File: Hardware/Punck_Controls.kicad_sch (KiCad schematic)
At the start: 34 parts, among them J1 Audio_In_L, J11 Conn_01x08_Female, J12 Conn_01x08_Female, J13 Conn_01x08_Female, J14 Conn_01x08_Female, J4 Audio_Out_R, J8 Audio_Out_L

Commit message: Rough Draft of Control PCB Done
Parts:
- removed BTN1, BTN2, BTN3, BTN4, BTN5, BTN6: SW_Push, Custom_Footprints:SW_PUSH_6mm_aligned, symbol Switch:SW_Push
- removed D?: LED_Dual_AKA, LED_THT:LED_D3.0mm-3, symbol Device:LED_Dual_AKA
- removed J11, J12, J13, J14: Conn_01x08_Female, Socket_Strips:Socket_Strip_Straight_1x08_Pitch2.54mm, symbol Connector:Conn_01x08_Female
- removed R? (x2): 1k, Resistor_SMD:R_0603_1608Metric, symbol Device:R_Small
- removed Snare_Decay_Pot1, Toms_Vol_Pot: B10k, Custom_Footprints:Alpha_9mm_Potentiometer_Aligned, symbol Device:R_POT
- added BTN1, BTN2, BTN3, BTN4, BTN5, BTN6: KS01-BLV, Custom_Footprints:KS01-BLV, symbol LED_Button_KS01-BLV:KS01-BLV
- added J1: (no value), symbol Connector:Conn_01x12_Female
- added J2, J3, J4: Conn_01x12_Female, symbol Connector:Conn_01x12_Female
- added J? (x5): (no value), Custom_Footprints:THONKICONN_hole, symbol thonkiconn:AudioJack2_Ground_Switch
- added SampleA_Voice_Pot1, SampleB_Voice_Pot1: B10k, Custom_Footprints:Alpha_9mm_Potentiometer_Aligned, symbol Device:R_POT
- J7: renamed from J1; value Audio_In_L -> Midi_In_L
- gave numbers to parts that had none: 7
- renumbered HiHat_Decay_Pot to HiHat_Decay_Pot1, J4 to J5, Kick_Filter_Pot1 to Kick_Attack_Pot1, Kick_Decay1 to Kick_Decay_Pot1, Sample_Speed_Pot1 to SampleB_Speed_Pot1
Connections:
- net +3.3VA: now also J1.1 (Pin_1), SampleA_Voice_Pot1.1, SampleB_Voice_Pot1.1
- net EXT_AUDIO_OUT_L: now also J4.11 (Pin_11)
- net EXT_AUDIO_OUT_R: now also J4.10 (Pin_10)
- net GND: now also BTN1.3, BTN1.4, BTN1.6 (K), BTN2.3, BTN2.4, BTN2.6 (K), BTN3.3, BTN3.4, BTN3.6 (K), BTN4.3, BTN4.4, BTN4.6 (K), BTN5.3, BTN5.4, BTN5.6 (K), BTN6.3, BTN6.4, BTN6.6 (K), J4.12 (Pin_12), J?.1, J?.1, J?.1, J?.1, J?.1, J?.2, J?.2, J?.2, J?.2, J?.2, SampleA_Voice_Pot1.3, SampleB_Voice_Pot1.3
- net HIHAT_DECAY_POT: now also J3.3 (Pin_3)
- net HIHAT_VOL_POT: now also J3.4 (Pin_4)
- net KICK_DECAY_POT: now also J2.6 (Pin_6)
- net KICK_VOL_POT: now also J2.7 (Pin_7)
- net MIDI_IN: now also J4.6 (Pin_6)
- net MIDI_LEARN: now also J4.7 (Pin_7)
- net SAMPLER_A_SPEED_POT: now also J3.6 (Pin_6)
- net SAMPLER_A_VOL_POT: now also J3.7 (Pin_7)
- net SAMPLER_B_SPEED_POT: now also J3.9 (Pin_9)
- net SAMPLER_B_VOL_POT: now also J3.10 (Pin_10)
- net SEQ_SELECT: now also J4.8 (Pin_8)
- net SNARE_FILTER_POT: now also J2.8 (Pin_8)
- net SNARE_TUNING_POT: now also J2.9 (Pin_9)
- net SNARE_VOL_POT: now also J2.10 (Pin_10)
- net TEMPO: now also J4.9 (Pin_9)
- net USB_DM: now also J4.4 (Pin_4)
- net USB_DP: now also J4.3 (Pin_3)
- net USB_VBUS: now also J4.5 (Pin_5)
- net KICK_FILTER_POT renamed KICK_ATTACK_POT
- net KICK_ATTACK_POT: now also J2.5 (Pin_5)
- new net CH_BTN: BTN3.1, BTN3.2, J1.7 (Pin_7)
- new net CH_LED: BTN3.5 (A), J1.8 (Pin_8)
- new net KICK_IN: J1.2 (Pin_2), J?.3
- new net KI_BTN: BTN1.1, BTN1.2
- new net KI_LED: BTN1.5 (A)
- new net OH_BTN: BTN6.1, BTN6.2, J1.5 (Pin_5)
- new net OH_IN: J2.2 (Pin_2), J?.3
- new net OH_LED: BTN6.5 (A), J1.6 (Pin_6)
- new net SAMPLERA_IN: J3.2 (Pin_2), J?.3
- new net SAMPLERB_IN: J4.2 (Pin_2), J?.3
- new net SAMPLER_A_VOICE_POT: J3.5 (Pin_5), SampleA_Voice_Pot1.2
- new net SAMPLER_B_VOICE_POT: J3.8 (Pin_8), SampleB_Voice_Pot1.2
- new net SA_BTN: BTN4.1, BTN4.2, J1.9 (Pin_9)
- new net SA_LED: BTN4.5 (A), J1.10 (Pin_10)
- new net SB_BTN: BTN5.1, BTN5.2, J2.3 (Pin_3)
- new net SB_LED: BTN5.5 (A), J2.4 (Pin_4)
- new net SNARE_IN: J1.11 (Pin_11), J?.3
- new net SN_BTN: BTN2.1, BTN2.2, J1.3 (Pin_3)
- new net SN_LED: BTN2.5 (A), J1.4 (Pin_4)
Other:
- note added: "System Controls"
- note added: "Voice Controls"
- note removed: "CV Inputs"
- note removed: "Switches and Buttons"
- moved on the sheet: BTN_MODE1, HiHat_Decay_Pot1, HiHat_Level_Pot1, J5, J6, J7, J8, Kick_Attack_Pot1, Kick_Decay_Pot1, Kick_Level_Pot1, RESET1, SampleA_Level_Pot1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

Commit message: First draft of Controls PCB
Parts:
- added J15: Audio_Out_R, Custom_Footprints:THONKICONN_hole, symbol thonkiconn:AudioJack2_Ground_Switch
- added J7: OH_In, Custom_Footprints:THONKICONN_hole, symbol thonkiconn:AudioJack2_Ground_Switch
- HiHat_Decay_Pot1, HiHat_Level_Pot1, Kick_Attack_Pot1, Kick_Decay_Pot1, Kick_Level_Pot1, SampleA_Level_Pot1, SampleA_Speed_Pot1, SampleA_Voice_Pot1, SampleB_Level_Pot1, SampleB_Speed_Pot1, SampleB_Voice_Pot1, Snare_Filter_Pot1, Snare_Level_Pot1, Snare_Tuning_Pot1, Tempo_Pot1: symbol Device:R_POT -> Encoder:R_POT
- J1: value (none) -> Conn_01x12_Female; footprint (none) -> Connector_PinHeader_2.54mm:PinHeader_1x12_P2.54mm_Vertical
- J10: renamed from J4; footprint (none) -> Connector_PinHeader_2.54mm:PinHeader_1x12_P2.54mm_Vertical
- J11: renamed from J5; value Audio_Out_R -> (none)
- J2, J3: footprint (none) -> Connector_PinHeader_2.54mm:PinHeader_1x12_P2.54mm_Vertical
- J4: renamed from J?; value (none) -> Kick_In
- J5: renamed from J?; value (none) -> Snare_In
- J6: renamed from J?; value (none) -> CH_In
- J8: renamed from J?; value (none) -> SamplerA_In
- J9: renamed from J?; value (none) -> SamplerB_In
- renumbered J6 to J12, J7 to J13, J8 to J14
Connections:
- net +3.3VA: now also J10.1 (Pin_1), J2.1 (Pin_1), J3.1 (Pin_1)
- net GND: now also J1.12 (Pin_12), J2.12 (Pin_12), J3.12 (Pin_12), J15.1, J7.1, J7.2
- net OH_IN: now also J7.3; no longer J2.2 (Pin_2), J6.3
- net TEMPO_OUT: now reaches J3.11 (Pin_11)
- net TEMPO_OUT: now also J11.3
- net EXT_AUDIO_OUT_L renamed AUDIO_OUT_L
- net EXT_AUDIO_OUT_R renamed AUDIO_OUT_R
- net AUDIO_OUT_R: now also J15.3; no longer J11.3
- net TEMPO renamed TEMPO_POT
- new net CH_IN: J2.2 (Pin_2), J6.3
- no-connect marks 2 -> 3
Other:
- note added: "HiHat"
- note added: "Kick"
- note added: "MIDI"
- note added: "Mode/Output"
- note added: "Sampler A"
- note added: "Sampler B"
- note added: "Snare"
- note added: "Tempo"
- note removed: "Outputs"
- note removed: "Potentiometers"
- note removed: "System Controls"
- note removed: "Voice Controls"
- title: Retrospector Control Board -> Punck Control Board
- moved on the sheet: BTN1, BTN2, BTN3, BTN4, BTN5, BTN6, BTN_MODE1, HiHat_Decay_Pot1, HiHat_Level_Pot1, J10, J11, J12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

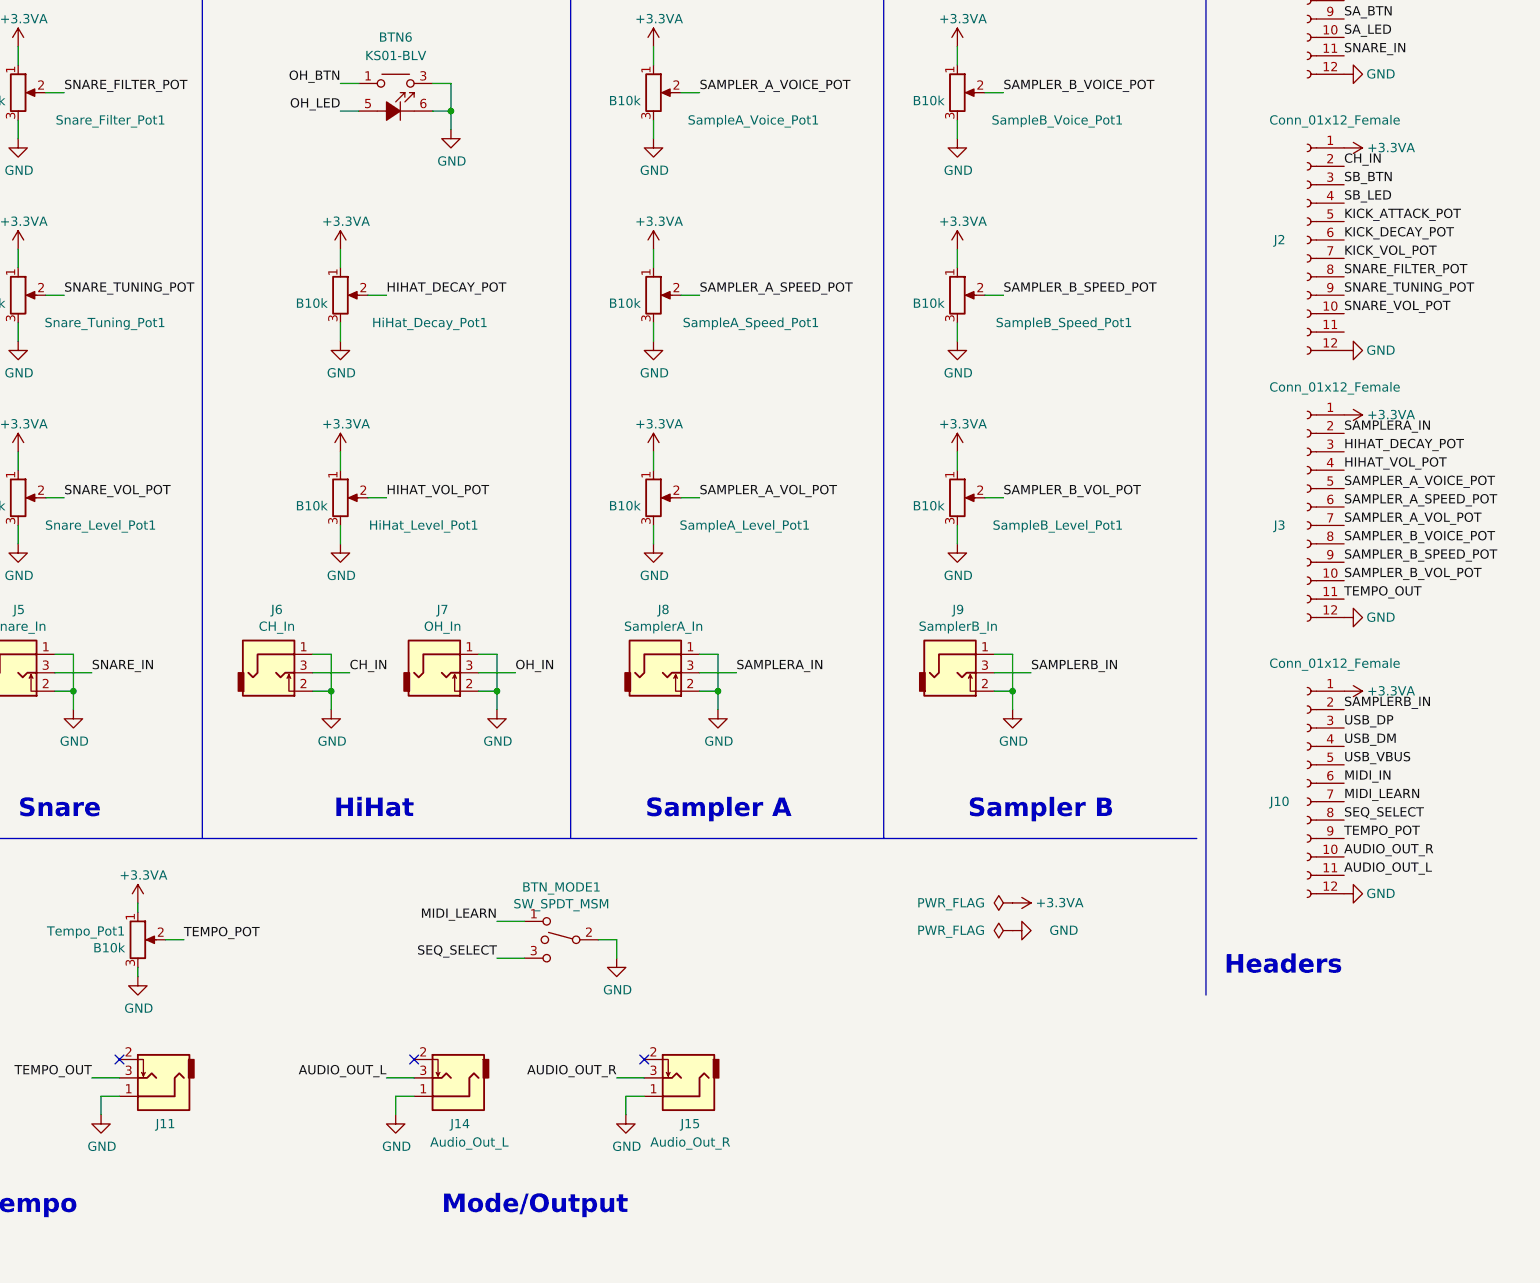
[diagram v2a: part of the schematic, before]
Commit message: Started component PCB
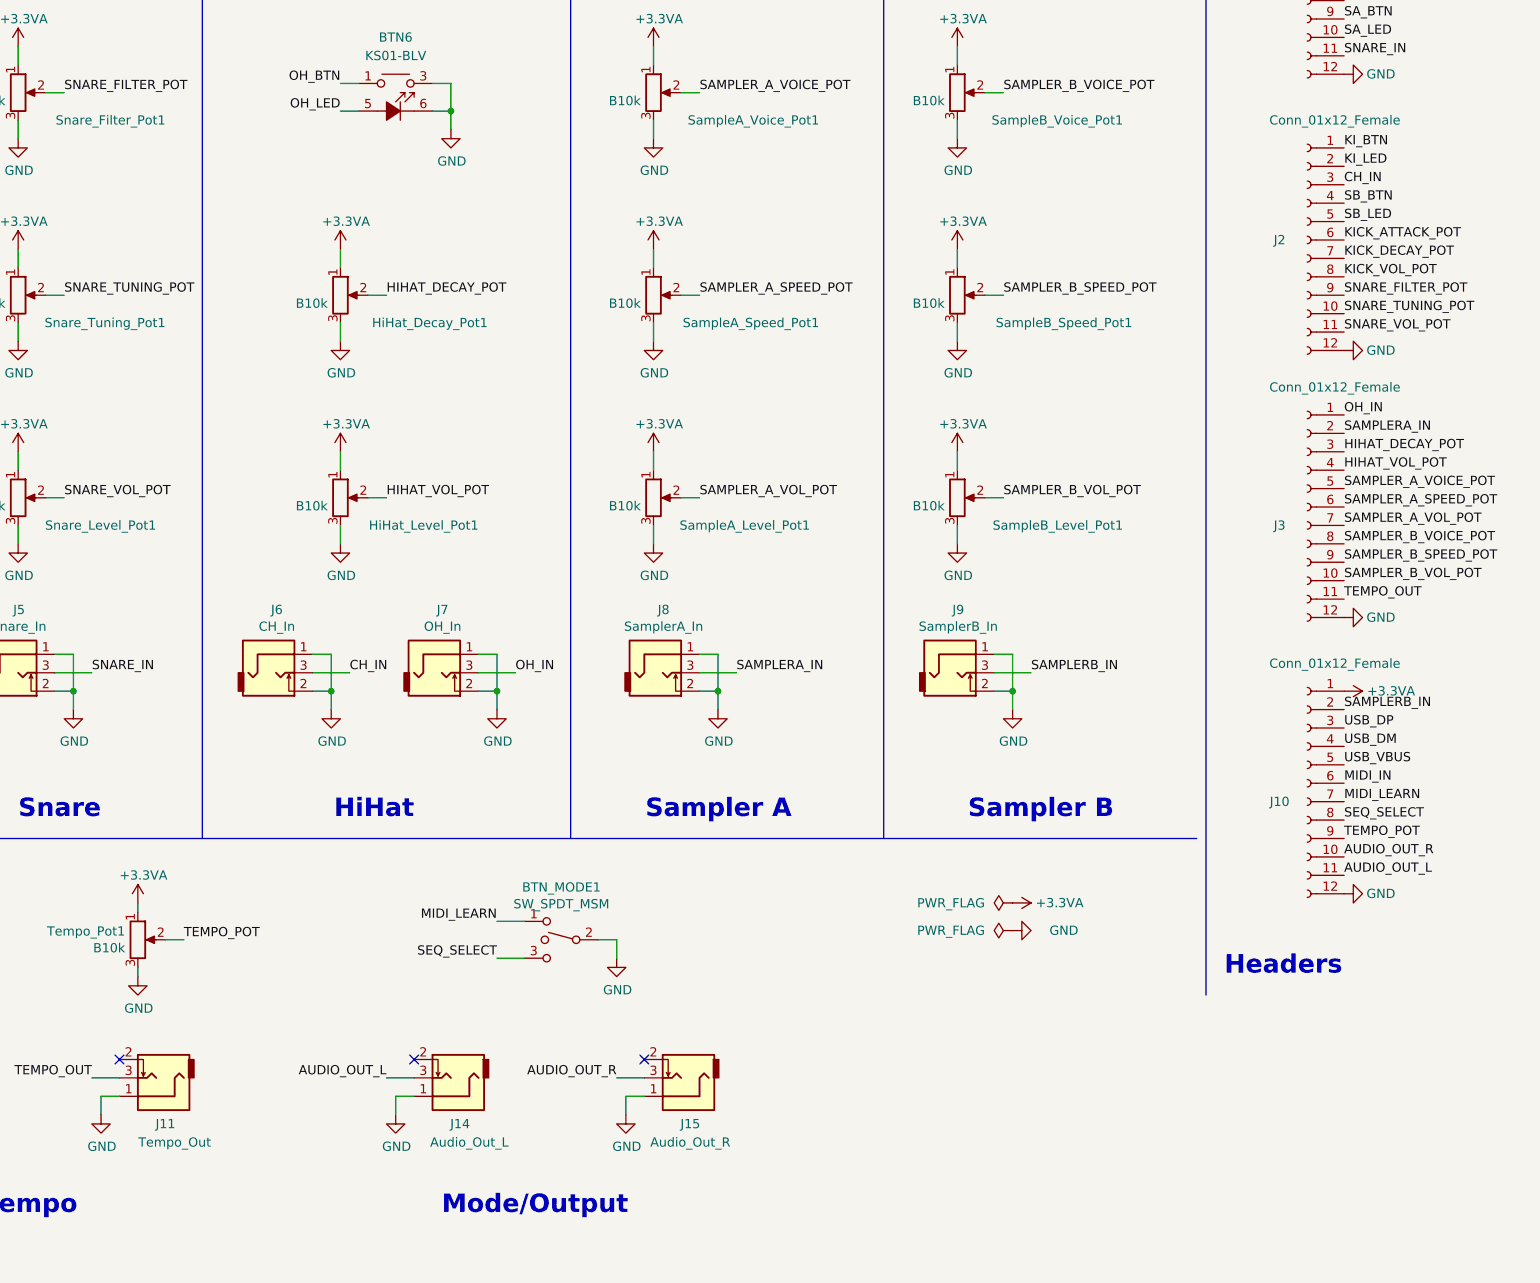
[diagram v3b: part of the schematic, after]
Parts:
- J11: value (none) -> Tempo_Out
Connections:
- net +3.3VA: no longer J2.1 (Pin_1), J3.1 (Pin_1)
- net CH_IN: now also J2.3 (Pin_3); no longer J2.2 (Pin_2)
- net KICK_ATTACK_POT: now also J2.6 (Pin_6); no longer J2.5 (Pin_5)
- net KICK_DECAY_POT: now also J2.7 (Pin_7); no longer J2.6 (Pin_6)
- net KICK_VOL_POT: now also J2.8 (Pin_8); no longer J2.7 (Pin_7)
- net KI_BTN: now also J2.1 (Pin_1)
- net KI_LED: now also J2.2 (Pin_2)
- net OH_IN: now also J3.1 (Pin_1)
- net SB_BTN: now also J2.4 (Pin_4); no longer J2.3 (Pin_3)
- net SB_LED: now also J2.5 (Pin_5); no longer J2.4 (Pin_4)
- net SNARE_FILTER_POT: now also J2.9 (Pin_9); no longer J2.8 (Pin_8)
- net SNARE_TUNING_POT: now also J2.10 (Pin_10); no longer J2.9 (Pin_9)
- net SNARE_VOL_POT: now also J2.11 (Pin_11); no longer J2.10 (Pin_10)
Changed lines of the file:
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@@
     (effects (font (size 1.27 1.27)) (justify left bottom))
   )
-  (label "SNARE_TUNING_POT" (at 252.73 78.74 0)
+  (label "SNARE_TUNING_POT" (at 252.73 81.28 0)
     (effects (font (size 1.27 1.27)) (justify left bottom))
   )
@@
     (effects (font (size 1.27 1.27)) (justify left bottom))
   )
-  (label "SNARE_FILTER_POT" (at 252.73 76.2 0)
+  (label "SNARE_FILTER_POT" (at 252.73 78.74 0)
     (effects (font (size 1.27 1.27)) (justify left bottom))
   )
   (label "MIDI_LEARN" (at 252.73 148.59 0)
+    (effects (font (size 1.27 1.27)) (justify left bottom))
+  )
+  (label "KI_BTN" (at 252.73 58.42 0)
     (effects (font (size 1.27 1.27)) (justify left bottom))
   )
@@
     (effects (font (size 1.27 1.27)) (justify left bottom))
   )
-  (label "SB_LED" (at 252.73 66.04 0)
+  (label "SB_LED" (at 252.73 68.58 0)
     (effects (font (size 1.27 1.27)) (justify left bottom))
   )
@@
     (effects (font (size 1.27 1.27)) (justify left bottom))
   )
+  (label "KI_LED" (at 252.73 60.96 0)
+    (effects (font (size 1.27 1.27)) (justify left bottom))
+  )
   (label "USB_DP" (at 25.4 165.1 180)
     (effects (font (size 1.27 1.27)) (justify right bottom))
@@
     (effects (font (size 1.27 1.27)) (justify left bottom))
   )
-  (label "CH_IN" (at 252.73 60.96 0)
+  (label "CH_IN" (at 252.73 63.5 0)
     (effects (font (size 1.27 1.27)) (justify left bottom))
   )
@@
     (effects (font (size 1.27 1.27)) (justify left bottom))
   )
-  (label "KICK_VOL_POT" (at 252.73 73.66 0)
+  (label "KICK_VOL_POT" (at 252.73 76.2 0)
     (effects (font (size 1.27 1.27)) (justify left bottom))
   )
@@
     (effects (font (size 1.27 1.27)) (justify left bottom))
   )
-  (label "KICK_ATTACK_POT" (at 252.73 68.58 0)
+  (label "KICK_ATTACK_POT" (at 252.73 71.12 0)
     (effects (font (size 1.27 1.27)) (justify left bottom))
   )
@@
     (effects (font (size 1.27 1.27)) (justify left bottom))
   )
+  (label "OH_IN" (at 252.73 95.25 0)
+    (effects (font (size 1.27 1.27)) (justify left bottom))
+  )
   (label "SN_BTN" (at 252.73 25.4 0)
     (effects (font (size 1.27 1.27)) (justify left bottom))
@@
     (effects (font (size 1.27 1.27)) (justify left bottom))
   )
-  (label "SNARE_VOL_POT" (at 252.73 81.28 0)
-    (effects (font (size 1.27 1.27)) (justify left bottom))
-  )
-  (label "SB_BTN" (at 252.73 63.5 0)
+  (label "SNARE_VOL_POT" (at 252.73 83.82 0)
+    (effects (font (size 1.27 1.27)) (justify left bottom))
+  )
+  (label "SB_BTN" (at 252.73 66.04 0)
     (effects (font (size 1.27 1.27)) (justify left bottom))
   )
@@
     (effects (font (size 1.27 1.27)) (justify left bottom))
   )
-  (label "KICK_DECAY_POT" (at 252.73 71.12 0)
+  (label "KICK_DECAY_POT" (at 252.73 73.66 0)
     (effects (font (size 1.27 1.27)) (justify left bottom))
   )
@@
     (in_bom yes) (on_board yes)
     (property "Reference" "J11" (id 0) (at 90.17 193.04 0))
-    (property "Value" "" (id 1) (at 91.44 195.58 0))
+    (property "Value" "Tempo_Out" (id 1) (at 91.44 195.58 0))
     (property "Footprint" "Custom_Footprints:THONKICONN_hole" (id 2) (at 88.9 186.69 0)
       (effects (font (size 1.27 1.27)) hide)
@@
     (pin "2")
     (pin "3")
-  )
-  (symbol (lib_id "power:+3.3VA") (at 252.73 95.25 270) (unit 1)
-    (in_bom yes) (on_board yes) (fields_autoplaced)
-    (property "Reference" "#PWR029" (id 0) (at 248.92 95.25 0)
-      (effects (font (size 1.27 1.27)) hide)
-    )
-    (property "Value" "+3.3VA" (id 1) (at 255.905 95.2499 90)
-      (effects (font (size 1.27 1.27)) (justify left))
-    )
-    (property "Footprint" "" (id 2) (at 252.73 95.25 0)
-      (effects (font (size 1.27 1.27)) hide)
-    )
-    (property "Datasheet" "" (id 3) (at 252.73 95.25 0)
-      (effects (font (size 1.27 1.27)) hide)
-    )
-    (pin "1")
   )
   (symbol (lib_id "power:GND") (at 157.48 85.09 0) (unit 1)
@@
     (pin "3")
   )
-  (symbol (lib_id "power:+3.3VA") (at 252.73 58.42 270) (unit 1)
-    (in_bom yes) (on_board yes) (fields_autoplaced)
-    (property "Reference" "#PWR017" (id 0) (at 248.92 58.42 0)
-      (effects (font (size 1.27 1.27)) hide)
-    )
-    (property "Value" "+3.3VA" (id 1) (at 255.905 58.4199 90)
-      (effects (font (size 1.27 1.27)) (justify left))
-    )
-    (property "Footprint" "" (id 2) (at 252.73 58.42 0)
-      (effects (font (size 1.27 1.27)) hide)
-    )
-    (property "Datasheet" "" (id 3) (at 252.73 58.42 0)
-      (effects (font (size 1.27 1.27)) hide)
-    )
-    (pin "1")
-  )
   (symbol (lib_id "Encoder:R_POT") (at 157.48 78.74 0) (unit 1)
     (in_bom yes) (on_board yes)
@@
       (reference "#PWR016") (unit 1) (value "GND") (footprint "")
     )
-    (path "/bfa74158-1e04-49f7-86c6-045eb3930242"
-      (reference "#PWR017") (unit 1) (value "+3.3VA") (footprint "")
-    )
     (path "/00000000-0000-0000-0000-00005f87431e"
       (reference "#PWR018") (unit 1) (value "+3.3VA") (footprint "")
@@
       (reference "#PWR028") (unit 1) (value "GND") (footprint "")
     )
-    (path "/391f1aed-beb7-4c2c-9d3d-7c44e394befd"
-      (reference "#PWR029") (unit 1) (value "+3.3VA") (footprint "")
-    )
     (path "/e28c66c9-88a4-4d53-ac7e-1cae7faf0a4d"
